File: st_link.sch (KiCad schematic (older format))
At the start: 29 parts, among them J1 USB_C_Receptacle_USB2.0, J2 Conn_01x05, Q1 AO3402, U1 AMS1117-3.3, U2 STM32F103C8Tx, Y1 8M

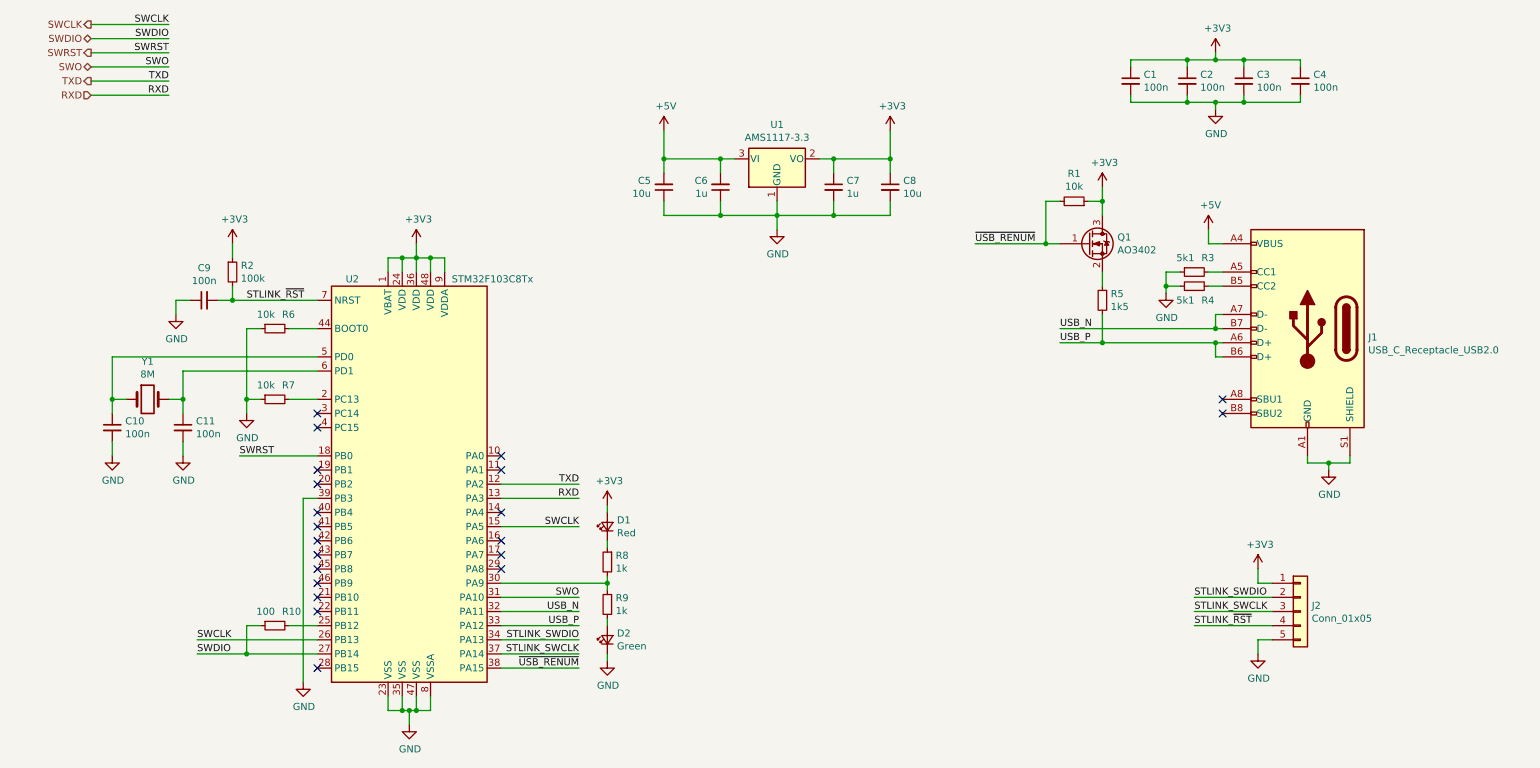
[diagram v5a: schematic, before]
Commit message: sch, pcb: Add USB hub to have a single USB port
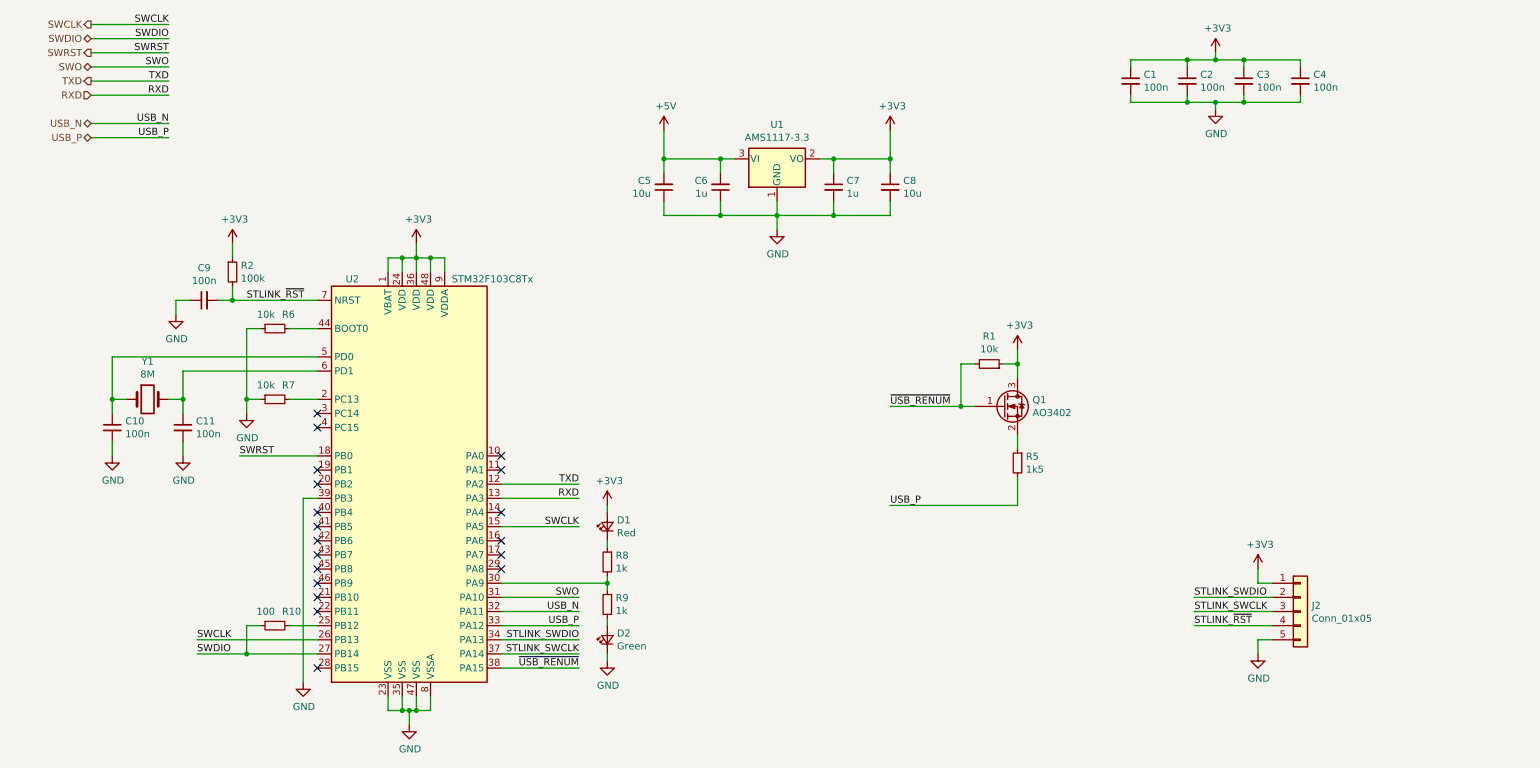
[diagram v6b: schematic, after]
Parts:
- removed J1: USB_C_Receptacle_USB2.0, antboard:USB_C_Receptacle_Palconn_UTC16-G, symbol Connector:USB_C_Receptacle_USB2.0
- removed R3, R4: 5k1, Resistor_SMD:R_0603_1608Metric, symbol Device:R_Small
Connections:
- no-connect marks 21 -> 19
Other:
- moved on the sheet: Q1, R1, R5
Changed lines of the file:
@@
 EESchema Schematic File Version 4
+LIBS:antboard-cache
 EELAYER 30 0
 EELAYER END
 $Descr A4 11693 8268
 encoding utf-8
-Sheet 2 5
+Sheet 2 6
 Title "STM32 devboard with .05\" headers"
 Date ""
@@
 Text Label 2450 4300 0    50   ~ 0
 SWRST
-$Comp
-L Connector:USB_C_Receptacle_USB2.0 J1
-U 1 1 5DFA8C64
-P 10000 3400
-F 0 "J1" H 9570 3339 50  0000 R CNN
-F 1 "USB_C_Receptacle_USB2.0" H 9570 3248 50  0000 R CNN
-F 2 "antboard:USB_C_Receptacle_Palconn_UTC16-G" H 10150 3400 50  0001 C CNN
-F 3 "https://www.usb.org/sites/default/files/documents/usb_type-c.zip" H 10150 3400 50  0001 C CNN
-	1    10000 3400
-	-1   0    0    -1
-$EndComp
 Wire Wire Line
 	4300 5400 4850 5400
@@
 Text Label 4850 5500 2    50   ~ 0
 USB_P
-Wire Wire Line
-	9400 3400 9350 3400
-Text Label 8250 3400 0    50   ~ 0
-USB_N
-Wire Wire Line
-	9400 3500 9350 3500
-Text Label 8250 3500 0    50   ~ 0
+Text Label 7050 4650 0    50   ~ 0
 USB_P
-Wire Wire Line
-	9400 3300 9350 3300
-Wire Wire Line
-	9350 3300 9350 3400
-Connection ~ 9350 3400
-Wire Wire Line
-	9350 3500 9350 3600
-Wire Wire Line
-	9350 3600 9400 3600
-Connection ~ 9350 3500
-NoConn ~ 9400 3900
-NoConn ~ 9400 4000
 Wire Wire Line
 	4300 5600 4850 5600
@@
 L power:+3V3 #PWR?
 U 1 1 5DFA8CA2
-P 8550 2400
+P 7950 3550
 AR Path="/5DFA8CA2" Ref="#PWR?"  Part="1"
 AR Path="/5DF7E971/5DFA8CA2" Ref="#PWR0109"  Part="1"
-F 0 "#PWR0109" H 8550 2250 50  0001 C CNN
-F 1 "+3V3" H 8565 2573 50  0000 C CNN
-F 2 "" H 8550 2400 50  0001 C CNN
-F 3 "" H 8550 2400 50  0001 C CNN
-	1    8550 2400
+F 0 "#PWR0109" H 7950 3400 50  0001 C CNN
+F 1 "+3V3" H 7965 3723 50  0000 C CNN
+F 2 "" H 7950 3550 50  0001 C CNN
+F 3 "" H 7950 3550 50  0001 C CNN
+	1    7950 3550
 	1    0    0    -1
 $EndComp
@@
 NoConn ~ 3000 5800
 $Comp
-L Device:R_Small R?
-U 1 1 5DFA8CBF
-P 9200 3000
-AR Path="/5DFA8CBF" Ref="R?"  Part="1"
-AR Path="/5DF7E971/5DFA8CBF" Ref="R3"  Part="1"
-F 0 "R3" V 9100 2950 50  0000 R CNN
-F 1 "5k1" V 9100 3000 50  0000 L CNN
-F 2 "Resistor_SMD:R_0603_1608Metric" H 9200 3000 50  0001 C CNN
-F 3 "~" H 9200 3000 50  0001 C CNN
-	1    9200 3000
-	0    -1   1    0
-$EndComp
-$Comp
-L Device:R_Small R?
-U 1 1 5DFA8CC5
-P 9200 3100
-AR Path="/5DFA8CC5" Ref="R?"  Part="1"
-AR Path="/5DF7E971/5DFA8CC5" Ref="R4"  Part="1"
-F 0 "R4" V 9100 3050 50  0000 R CNN
-F 1 "5k1" V 9100 3100 50  0000 L CNN
-F 2 "Resistor_SMD:R_0603_1608Metric" H 9200 3100 50  0001 C CNN
-F 3 "~" H 9200 3100 50  0001 C CNN
-	1    9200 3100
-	0    -1   -1   0
-$EndComp
-Wire Wire Line
-	9300 3000 9400 3000
-Wire Wire Line
-	9300 3100 9400 3100
-Wire Wire Line
-	9100 3000 9000 3000
-Wire Wire Line
-	9000 3000 9000 3100
-$Comp
-L power:GND #PWR?
-U 1 1 5DFA8CCF
-P 9000 3150
-AR Path="/5DFA8CCF" Ref="#PWR?"  Part="1"
-AR Path="/5DF7E971/5DFA8CCF" Ref="#PWR0110"  Part="1"
-F 0 "#PWR0110" H 9000 2900 50  0001 C CNN
-F 1 "GND" H 9005 2977 50  0000 C CNN
-F 2 "" H 9000 3150 50  0001 C CNN
-F 3 "" H 9000 3150 50  0001 C CNN
-	1    9000 3150
-	1    0    0    -1
-$EndComp
-Wire Wire Line
-	9000 3100 9100 3100
-Connection ~ 9000 3100
-Wire Wire Line
-	9000 3100 9000 3150
-$Comp
-L power:GND #PWR?
-U 1 1 5DFA8CD8
-P 10150 4400
-AR Path="/5DFA8CD8" Ref="#PWR?"  Part="1"
-AR Path="/5DF7E971/5DFA8CD8" Ref="#PWR0111"  Part="1"
-F 0 "#PWR0111" H 10150 4150 50  0001 C CNN
-F 1 "GND" H 10155 4227 50  0000 C CNN
-F 2 "" H 10150 4400 50  0001 C CNN
-F 3 "" H 10150 4400 50  0001 C CNN
-	1    10150 4400
-	1    0    0    -1
-$EndComp
-Wire Wire Line
-	10000 4300 10000 4350
-Wire Wire Line
-	10000 4350 10150 4350
-Wire Wire Line
-	10300 4350 10300 4300
-Wire Wire Line
-	10150 4400 10150 4350
-Connection ~ 10150 4350
-Wire Wire Line
-	10150 4350 10300 4350
-$Comp
 L antboard:AO3402 Q?
 U 1 1 5DFA8CE4
-P 8450 2800
+P 7850 3950
 AR Path="/5DFA8CE4" Ref="Q?"  Part="1"
 AR Path="/5DF7E971/5DFA8CE4" Ref="Q1"  Part="1"
-F 0 "Q1" H 8656 2846 50  0000 L CNN
-F 1 "AO3402" H 8656 2755 50  0000 L CNN
-F 2 "Package_TO_SOT_SMD:SOT-23" H 8650 2725 50  0001 L CIN
-F 3 "http://www.aosmd.com/pdfs/datasheet/AO3402.pdf" H 8450 2800 50  0001 L CNN
-	1    8450 2800
+F 0 "Q1" H 8056 3996 50  0000 L CNN
+F 1 "AO3402" H 8056 3905 50  0000 L CNN
+F 2 "Package_TO_SOT_SMD:SOT-23" H 8050 3875 50  0001 L CIN
+F 3 "http://www.aosmd.com/pdfs/datasheet/AO3402.pdf" H 7850 3950 50  0001 L CNN
+	1    7850 3950
 	1    0    0    -1
 $EndComp
@@
 L Device:R_Small R?
 U 1 1 5DFA8CEA
-P 8550 3200
+P 7950 4350
 AR Path="/5DFA8CEA" Ref="R?"  Part="1"
 AR Path="/5DF7E971/5DFA8CEA" Ref="R5"  Part="1"
-F 0 "R5" H 8491 3246 50  0000 R CNN
-F 1 "1k5" H 8491 3155 50  0000 R CNN
-F 2 "Resistor_SMD:R_0603_1608Metric" H 8550 3200 50  0001 C CNN
-F 3 "~" H 8550 3200 50  0001 C CNN
-	1    8550 3200
+F 0 "R5" H 7891 4396 50  0000 R CNN
+F 1 "1k5" H 7891 4305 50  0000 R CNN
+F 2 "Resistor_SMD:R_0603_1608Metric" H 7950 4350 50  0001 C CNN
+F 3 "~" H 7950 4350 50  0001 C CNN
+	1    7950 4350
 	-1   0    0    -1
 $EndComp
@@
 L Device:R_Small R?
 U 1 1 5DFA8CF0
-P 8350 2500
+P 7750 3650
 AR Path="/5DFA8CF0" Ref="R?"  Part="1"
 AR Path="/5DF7E971/5DFA8CF0" Ref="R1"  Part="1"
-F 0 "R1" V 8546 2500 50  0000 C CNN
-F 1 "10k" V 8455 2500 50  0000 C CNN
-F 2 "Resistor_SMD:R_0603_1608Metric" H 8350 2500 50  0001 C CNN
-F 3 "~" H 8350 2500 50  0001 C CNN
-	1    8350 2500
+F 0 "R1" V 7946 3650 50  0000 C CNN
+F 1 "10k" V 7855 3650 50  0000 C CNN
+F 2 "Resistor_SMD:R_0603_1608Metric" H 7750 3650 50  0001 C CNN
+F 3 "~" H 7750 3650 50  0001 C CNN
+	1    7750 3650
 	0    1    -1   0
 $EndComp
@@
 $EndComp
 Wire Wire Line
-	8450 2500 8550 2500
-Wire Wire Line
-	8550 2500 8550 2600
-Wire Wire Line
-	8550 2500 8550 2400
-Connection ~ 8550 2500
-Wire Wire Line
-	8250 2500 8150 2500
-Wire Wire Line
-	8150 2500 8150 2800
-Wire Wire Line
-	8150 2800 8250 2800
-Wire Wire Line
-	8150 2800 7650 2800
-Connection ~ 8150 2800
-Wire Wire Line
-	8550 3000 8550 3100
-Wire Wire Line
-	8250 3400 9350 3400
-Wire Wire Line
-	8550 3300 8550 3500
-Wire Wire Line
-	8250 3500 8550 3500
-Connection ~ 8550 3500
-Wire Wire Line
-	8550 3500 9350 3500
-Text Label 7650 2800 0    50   ~ 0
+	7850 3650 7950 3650
+Wire Wire Line
+	7950 3650 7950 3750
+Wire Wire Line
+	7950 3650 7950 3550
+Connection ~ 7950 3650
+Wire Wire Line
+	7650 3650 7550 3650
+Wire Wire Line
+	7550 3650 7550 3950
+Wire Wire Line
+	7550 3950 7650 3950
+Wire Wire Line
+	7550 3950 7050 3950
+Connection ~ 7550 3950
+Wire Wire Line
+	7950 4150 7950 4250
+Wire Wire Line
+	7950 4450 7950 4650
+Wire Wire Line
+	7050 4650 7950 4650
+Text Label 7050 3950 0    50   ~ 0
 ~USB_RENUM
-$Comp
-L power:+5V #PWR?
-U 1 1 5DFA8D0C
-P 9300 2700
-AR Path="/5DFA8D0C" Ref="#PWR?"  Part="1"
-AR Path="/5DF7E971/5DFA8D0C" Ref="#PWR0113"  Part="1"
-F 0 "#PWR0113" H 9300 2550 50  0001 C CNN
-F 1 "+5V" H 9315 2873 50  0000 C CNN
-F 2 "" H 9300 2700 50  0001 C CNN
-F 3 "" H 9300 2700 50  0001 C CNN
-	1    9300 2700
-	1    0    0    -1
-$EndComp
-Wire Wire Line
-	9300 2700 9300 2800
-Wire Wire Line
-	9300 2800 9400 2800
 $Comp
 L Device:C_Small C?
@@
 Text HLabel 1400 1750 0    50   Input ~ 0
 RXD
+Wire Wire Line
+	1400 1950 1950 1950
+Text Label 1950 1950 2    50   ~ 0
+USB_N
+Wire Wire Line
+	1400 2050 1950 2050
+Text Label 1950 2050 2    50   ~ 0
+USB_P
+Text HLabel 1400 1950 0    50   BiDi ~ 0
+USB_N
+Text HLabel 1400 2050 0    50   BiDi ~ 0
+USB_P
 $EndSCHEMATC

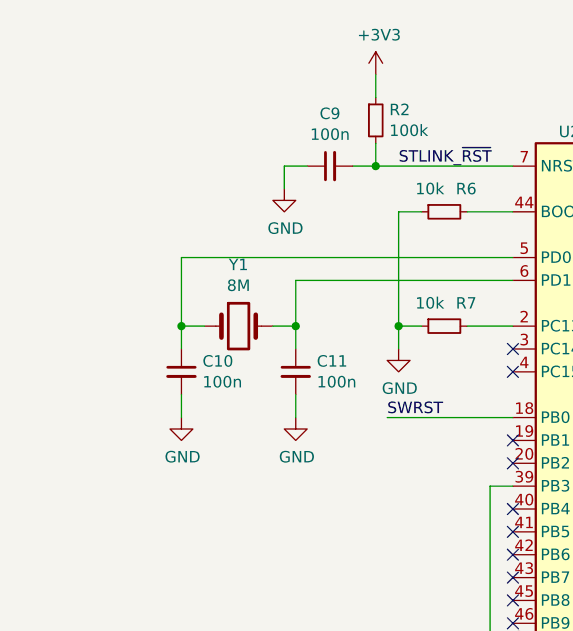
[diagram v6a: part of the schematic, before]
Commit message: sch, pcb: Fix hub startup and use smaller crystals
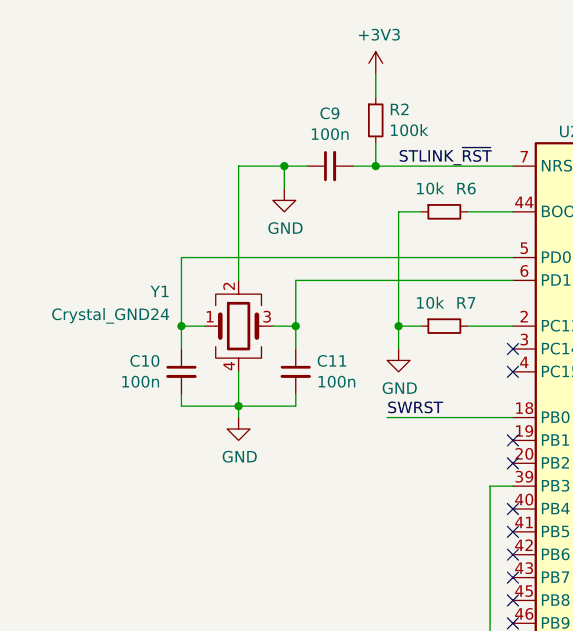
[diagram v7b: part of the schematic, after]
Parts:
- removed Y1: 8M, Crystal:Crystal_HC49-4H_Vertical, symbol Device:Crystal
- added Y1: Crystal_GND24, Crystal:Crystal_SMD_3225-4Pin_3.2x2.5mm, symbol Device:Crystal_GND24
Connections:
- net GND: now also Y1.2, Y1.4
- net at C10.1, U2.5 (PD0): now also Y1.1
- net at C11.1, U2.6 (PD1): now also Y1.3
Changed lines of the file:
@@
 NoConn ~ 3000 4100
-$Comp
-L Device:Crystal Y1
-U 1 1 5DFA8C19
-P 1800 3900
-F 0 "Y1" H 1800 4168 50  0000 C CNN
-F 1 "8M" H 1800 4077 50  0000 C CNN
-F 2 "Crystal:Crystal_HC49-4H_Vertical" H 1800 3900 50  0001 C CNN
-F 3 "~" H 1800 3900 50  0001 C CNN
-	1    1800 3900
-	1    0    0    -1
-$EndComp
 $Comp
 L Device:C_Small C10
 U 1 1 5DFA8C1F
 P 1550 4100
-F 0 "C10" H 1458 4146 50  0000 R CNN
-F 1 "100n" H 1458 4055 50  0000 R CNN
+F 0 "C10" H 1642 4146 50  0000 L CNN
+F 1 "100n" H 1642 4055 50  0000 L CNN
 F 2 "Capacitor_SMD:C_0603_1608Metric" H 1550 4100 50  0001 C CNN
 F 3 "~" H 1550 4100 50  0001 C CNN
@@
 	2050 3900 2050 4000
 Connection ~ 2050 3900
-$Comp
-L power:GND #PWR0105
-U 1 1 5DFA8C35
-P 2050 4300
-F 0 "#PWR0105" H 2050 4050 50  0001 C CNN
-F 1 "GND" H 2055 4127 50  0000 C CNN
-F 2 "" H 2050 4300 50  0001 C CNN
-F 3 "" H 2050 4300 50  0001 C CNN
-	1    2050 4300
-	1    0    0    -1
-$EndComp
-$Comp
-L power:GND #PWR0106
-U 1 1 5DFA8C3B
-P 1550 4300
-F 0 "#PWR0106" H 1550 4050 50  0001 C CNN
-F 1 "GND" H 1555 4127 50  0000 C CNN
-F 2 "" H 1550 4300 50  0001 C CNN
-F 3 "" H 1550 4300 50  0001 C CNN
-	1    1550 4300
-	1    0    0    -1
-$EndComp
-Wire Wire Line
-	1550 4200 1550 4300
-Wire Wire Line
-	2050 4200 2050 4300
+Wire Wire Line
+	1550 4200 1550 4250
+Wire Wire Line
+	2050 4200 2050 4250
 $Comp
 L power:GND #PWR0107
@@
 Text HLabel 1400 2050 0    50   BiDi ~ 0
 USB_P
+$Comp
+L Device:Crystal_GND24 Y1
+U 1 1 5EE93ED7
+P 1800 3900
+F 0 "Y1" H 1500 4050 50  0000 R CNN
+F 1 "Crystal_GND24" H 1500 3950 50  0000 R CNN
+F 2 "Crystal:Crystal_SMD_3225-4Pin_3.2x2.5mm" H 1800 3900 50  0001 C CNN
+F 3 "~" H 1800 3900 50  0001 C CNN
+	1    1800 3900
+	1    0    0    -1
+$EndComp
+$Comp
+L power:GND #PWR061
+U 1 1 5EE960DF
+P 1800 4300
+F 0 "#PWR061" H 1800 4050 50  0001 C CNN
+F 1 "GND" H 1805 4127 50  0000 C CNN
+F 2 "" H 1800 4300 50  0001 C CNN
+F 3 "" H 1800 4300 50  0001 C CNN
+	1    1800 4300
+	1    0    0    -1
+$EndComp
+Wire Wire Line
+	1800 4100 1800 4250
+Wire Wire Line
+	1800 3700 1800 3200
+Wire Wire Line
+	1800 3200 2000 3200
+Connection ~ 2000 3200
+Wire Wire Line
+	1550 4250 1800 4250
+Connection ~ 1800 4250
+Wire Wire Line
+	1800 4250 1800 4300
+Wire Wire Line
+	1800 4250 2050 4250
 $EndSCHEMATC
